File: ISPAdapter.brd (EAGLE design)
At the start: 76 x 38 mm, 9 parts, among them U1 SWITCH_IC_QUAD74LVC4066

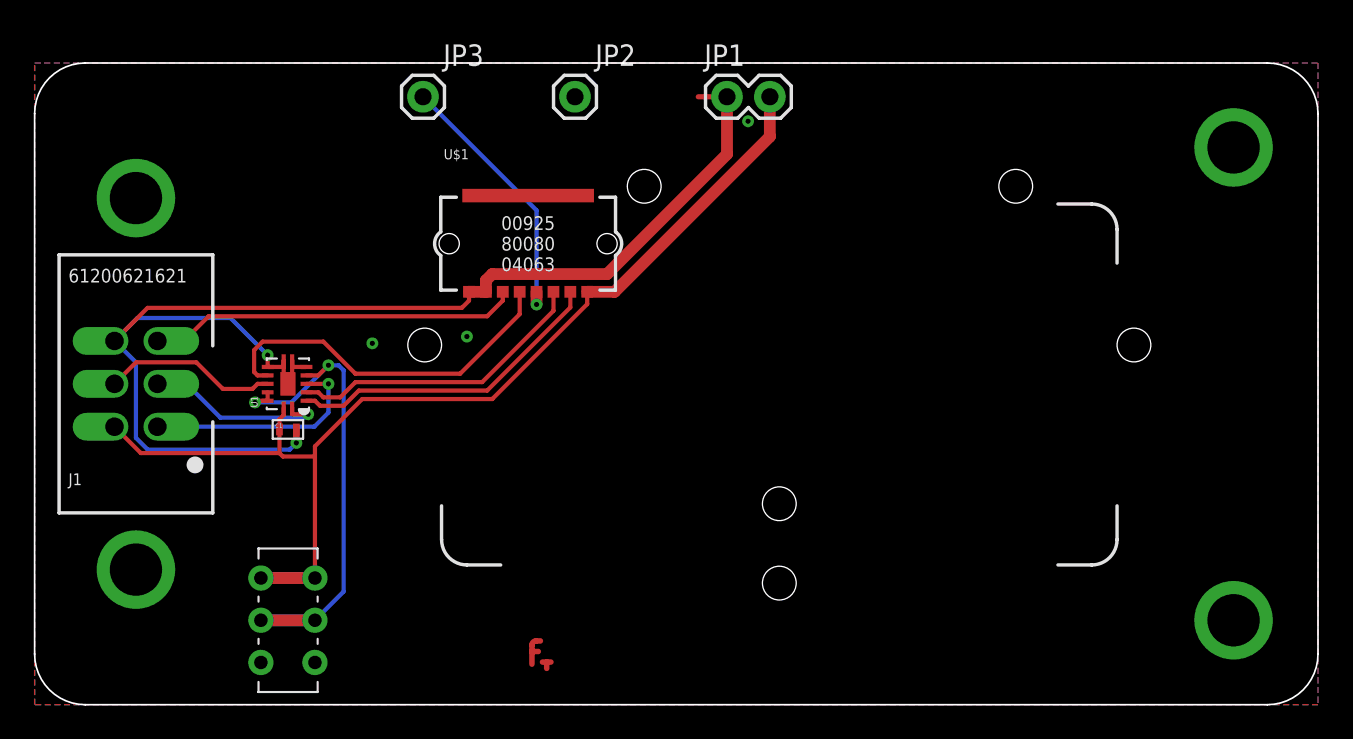
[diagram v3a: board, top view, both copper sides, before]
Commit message: Added cap to switch
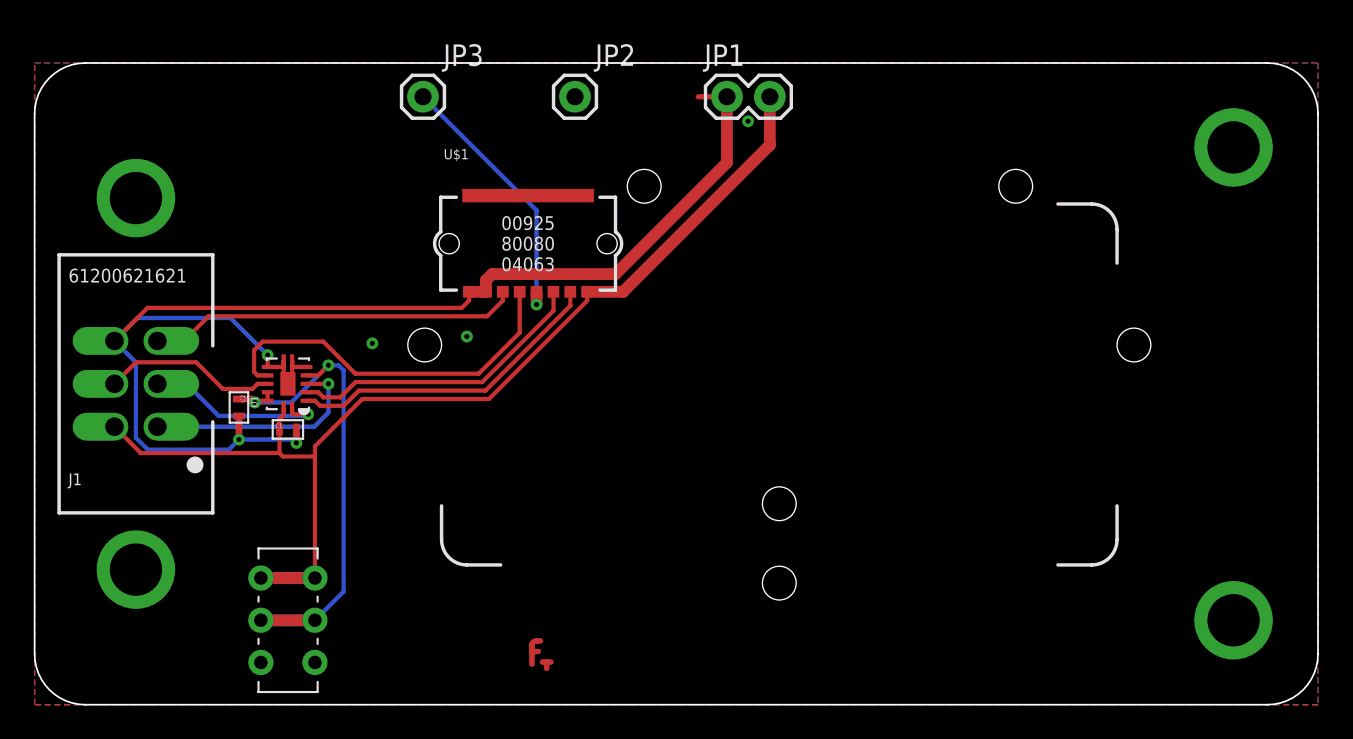
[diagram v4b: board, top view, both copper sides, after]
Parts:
- added C2: (no value), dubec:0402
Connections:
- net DGND: now also C2.2
- net ISP_EN: now also C2.1
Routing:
- net DGND: track 78.8 -> 80.7 mm, vias 2 -> 3
- net ISP_EN: track 31.0 -> 32.1 mm
- net MOSI: track 21.7 -> 22.3 mm
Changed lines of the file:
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@@
 <attribute name="TEMP" value="X5R" x="15" y="16.3" size="1.778" layer="27" display="off"/>
+</element>
+<element name="C2" library="dubec" package="0402" value="" x="12.1" y="17.6" rot="R270">
+<attribute name="TEMP" value="X5R" x="12.1" y="17.6" size="1.778" layer="27" rot="R270" display="off"/>
+<attribute name="TOLERANCE" value="±10%" x="12.1" y="17.6" size="1.778" layer="27" rot="R270" display="off"/>
+<attribute name="MFG_PART_#" value="GRM155R62A104KE14D" x="12.1" y="17.6" size="1.778" layer="27" rot="R270" display="off"/>
+<attribute name="DIGIKEY_PART_#" value="490-10458-1-ND" x="12.1" y="17.6" size="1.778" layer="27" rot="R270" display="off"/>
+<attribute name="MANUFACTURER" value="Murata Electronics North America" x="12.1" y="17.6" size="1.778" layer="27" rot="R270" display="off"/>
+<attribute name="USD" value="0.65/10" x="12.1" y="17.6" size="1.778" layer="27" rot="R270" display="off"/>
 </element>
 </elements>
@@
 <contactref element="U$1" pad="1"/>
 <contactref element="U1" pad="14"/>
-<wire x1="32.725" y1="24.45" x2="34.35" y2="24.45" width="0.7" layer="1"/>
-<wire x1="34.35" y1="24.45" x2="43.54" y2="33.64" width="0.7" layer="1"/>
-<wire x1="43.54" y1="33.64" x2="43.54" y2="36" width="0.7" layer="1"/>
-<wire x1="32.725" y1="23.725" x2="27.1" y2="18.1" width="0.25" layer="1"/>
-<wire x1="27.1" y1="18.1" x2="19.4" y2="18.1" width="0.25" layer="1"/>
+<wire x1="32.725" y1="24.45" x2="34.85" y2="24.45" width="0.7" layer="1"/>
+<wire x1="34.85" y1="24.45" x2="43.54" y2="33.14" width="0.7" layer="1"/>
+<wire x1="43.54" y1="33.14" x2="43.54" y2="36" width="0.7" layer="1"/>
+<wire x1="32.725" y1="23.925" x2="26.9" y2="18.1" width="0.25" layer="1"/>
+<wire x1="26.9" y1="18.1" x2="19.4" y2="18.1" width="0.25" layer="1"/>
 <contactref element="S1" pad="1"/>
 <contactref element="S1" pad="4"/>
 <wire x1="13.4" y1="7.5" x2="16.6" y2="7.5" width="0.7" layer="16"/>
 <wire x1="13.4" y1="7.5" x2="16.6" y2="7.5" width="0.7" layer="1"/>
-<wire x1="32.725" y1="23.725" x2="32.725" y2="24.45" width="0.25" layer="1"/>
+<wire x1="32.725" y1="23.925" x2="32.725" y2="24.45" width="0.25" layer="1"/>
 <wire x1="4.73" y1="16.46" x2="6.29" y2="14.9" width="0.25" layer="1"/>
 <wire x1="6.29" y1="14.9" x2="14.5" y2="14.9" width="0.25" layer="1"/>
@@
 <signal name="MOSI">
 <contactref element="U$1" pad="5"/>
-<wire x1="28.725" y1="24.45" x2="28.725" y2="23.125" width="0.25" layer="1"/>
-<wire x1="28.725" y1="23.125" x2="25.2" y2="19.6" width="0.25" layer="1"/>
+<wire x1="28.725" y1="24.45" x2="28.725" y2="22.025" width="0.25" layer="1"/>
+<wire x1="28.725" y1="22.025" x2="26.3" y2="19.6" width="0.25" layer="1"/>
 <contactref element="U1" pad="10"/>
-<wire x1="25.2" y1="19.6" x2="19" y2="19.6" width="0.25" layer="1"/>
+<wire x1="26.3" y1="19.6" x2="19" y2="19.6" width="0.25" layer="1"/>
 <wire x1="19" y1="19.6" x2="17.1" y2="21.5" width="0.25" layer="1"/>
 <wire x1="13" y1="19.7" x2="13.2" y2="19.5" width="0.25" layer="1"/>
@@
 <wire x1="27.1" y1="25.5" x2="26.725" y2="25.125" width="0.7" layer="1"/>
 <contactref element="U$1" pad="7"/>
-<wire x1="27.1" y1="25.5" x2="33.9" y2="25.5" width="0.7" layer="1"/>
-<wire x1="33.9" y1="25.5" x2="41" y2="32.6" width="0.7" layer="1"/>
-<wire x1="41" y1="32.6" x2="41" y2="36" width="0.7" layer="1"/>
+<wire x1="27.1" y1="25.5" x2="34.4" y2="25.5" width="0.7" layer="1"/>
+<wire x1="34.4" y1="25.5" x2="41" y2="32.1" width="0.7" layer="1"/>
+<wire x1="41" y1="32.1" x2="41" y2="36" width="0.7" layer="1"/>
 <wire x1="25.725" y1="23.925" x2="25.3" y2="23.5" width="0.25" layer="1"/>
 <wire x1="25.3" y1="23.5" x2="6.69" y2="23.5" width="0.25" layer="1"/>
@@
 <wire x1="6" y1="20.27" x2="6" y2="15.8" width="0.25" layer="16"/>
 <wire x1="6" y1="15.8" x2="6.7" y2="15.1" width="0.25" layer="16"/>
-<wire x1="6.7" y1="15.1" x2="15.1" y2="15.1" width="0.25" layer="16"/>
-<wire x1="15.1" y1="15.1" x2="15.5" y2="15.5" width="0.25" layer="16"/>
 <wire x1="6" y1="20.27" x2="4.73" y2="21.54" width="0.25" layer="16"/>
 <wire x1="13.8" y1="20.7" x2="11.6" y2="22.9" width="0.25" layer="16"/>
@@
 <wire x1="25.725" y1="23.925" x2="25.725" y2="24.45" width="0.25" layer="1"/>
 <wire x1="26.725" y1="24.45" x2="25.725" y2="24.45" width="0.7" layer="1"/>
+<contactref element="C2" pad="2"/>
+<via x="12.1" y="15.7" extent="1-16" drill="0.3"/>
+<wire x1="6.7" y1="15.1" x2="11.5" y2="15.1" width="0.25" layer="16"/>
+<wire x1="11.5" y1="15.1" x2="12.1" y2="15.7" width="0.25" layer="16"/>
+<wire x1="12.1" y1="15.7" x2="15.3" y2="15.7" width="0.25" layer="16"/>
+<wire x1="15.3" y1="15.7" x2="15.5" y2="15.5" width="0.25" layer="16"/>
+<wire x1="12.1" y1="15.7" x2="12.1" y2="17.1" width="0.4" layer="1"/>
 </signal>
 <signal name="MISO">
@@
 <signal name="SCK">
 <contactref element="U$1" pad="2"/>
-<wire x1="31.725" y1="23.525" x2="26.8" y2="18.6" width="0.25" layer="1"/>
-<wire x1="26.8" y1="18.6" x2="19.2" y2="18.6" width="0.25" layer="1"/>
-<wire x1="31.725" y1="23.525" x2="31.725" y2="24.45" width="0.25" layer="1"/>
+<wire x1="31.725" y1="23.625" x2="26.7" y2="18.6" width="0.25" layer="1"/>
+<wire x1="26.7" y1="18.6" x2="19.2" y2="18.6" width="0.25" layer="1"/>
+<wire x1="31.725" y1="23.625" x2="31.725" y2="24.45" width="0.25" layer="1"/>
 <contactref element="U1" pad="2"/>
 <wire x1="19.2" y1="18.6" x2="18.3" y2="17.7" width="0.25" layer="1"/>
@@
 <wire x1="18.3" y1="19.8" x2="18" y2="20.1" width="0.25" layer="16"/>
 <wire x1="18" y1="20.1" x2="17.4" y2="20.1" width="0.25" layer="16"/>
+<contactref element="C2" pad="1"/>
+<wire x1="13.05" y1="17.9" x2="12.85" y2="18.1" width="0.4" layer="1"/>
+<wire x1="12.85" y1="18.1" x2="12.1" y2="18.1" width="0.4" layer="1"/>
 </signal>
 <signal name="SCK_A">
@@
 <wire x1="15.25" y1="17.2" x2="16.2" y2="17.2" width="0.25" layer="1"/>
 <wire x1="7.27" y1="19" x2="9" y2="19" width="0.25" layer="16"/>
-<wire x1="9" y1="19" x2="11" y2="17" width="0.25" layer="16"/>
-<wire x1="11" y1="17" x2="16" y2="17" width="0.25" layer="16"/>
-<wire x1="16" y1="17" x2="16.2" y2="17.2" width="0.25" layer="16"/>
+<wire x1="9" y1="19" x2="10.9" y2="17.1" width="0.25" layer="16"/>
+<wire x1="10.9" y1="17.1" x2="16.1" y2="17.1" width="0.25" layer="16"/>
+<wire x1="16.1" y1="17.1" x2="16.2" y2="17.2" width="0.25" layer="16"/>
 </signal>
 <signal name="MISO_A">

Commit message: TSSOP
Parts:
- U1: value SWITCH_IC_QUAD74LVC4066 -> 74LVC4066PW; device dubec:14-VFQFN -> dubec:14-TSSOP
- moved C1 5.00 mm to (19.9, 17.3), turned to 180 degrees
- moved C2 2.77 mm to (12.4, 20.4), turned to 90 degrees
- moved U1 1.00 mm to (16.0, 19.0), turned to 270 degrees
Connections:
- removed net MISO_A: J1.1, U1.4
- removed net MOSI_A: J1.4, U1.11
- removed net SCK_A: J1.3, U1.1
- new net MISO_PROG: J1.1, U1.8
- new net MOSI_PROG: J1.4, U1.4
- new net SCK_PROG: J1.3, U1.11
- net DGND: now also U1.1, U1.13, U1.2; no longer U1.6, U1.8, U1.9, U1.PAD
- net ISP_EN: now also U1.6; no longer U1.13
- net MISO: now also U1.9; no longer U1.3
- net MOSI: now also U1.3; no longer U1.10
- net SCK: now also U1.10; no longer U1.2
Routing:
- net DGND: track 80.7 -> 64.0 mm, vias 3 -> 4
- net SCK_PROG: track 0.00 -> 14.8 mm
- net MOSI_PROG: track 0.00 -> 14.0 mm
- net MISO_A: track 13.5 -> 0.00 mm, vias 1 -> 0
- net SCK_A: track 11.1 -> 0.00 mm, vias 1 -> 0
- net MOSI_A: track 10.4 -> 0.00 mm
- net MOSI: track 22.3 -> 13.8 mm
- net MISO_PROG: track 0.00 -> 7.49 mm
- net MISO: track 18.0 -> 21.1 mm
- net SCK: track 19.0 -> 21.2 mm
- net ISP_EN: track 32.1 -> 30.5 mm
- net VCC: track 67.1 -> 65.6 mm
- net GND: vias 7 -> 8
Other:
- board text added: "PB3"
- board text removed: "AUX"
